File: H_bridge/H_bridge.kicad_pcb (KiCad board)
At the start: 4 copper layers, 100 x 100 mm, 18 parts, among them J1 Conn_01x10_Pin, J10 Conn_Coaxial, J11 Conn_Coaxial, J12 Conn_01x04_Pin, J2 Conn_01x10_Pin, J3 Conn_01x04_Pin, J4 Conn_01x05, J5 Conn_01x03, J6 Conn_Coaxial, J7 Conn_Coaxial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

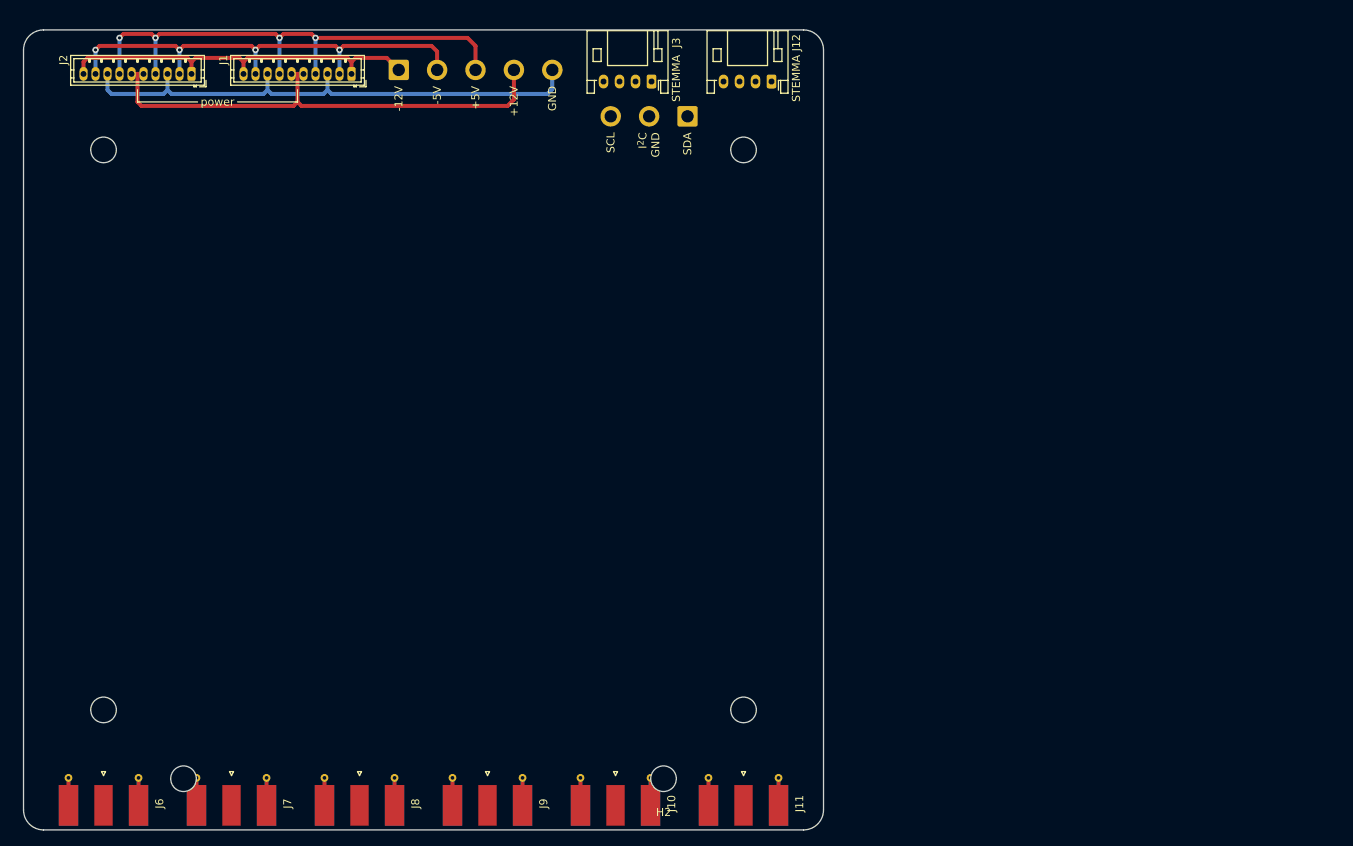
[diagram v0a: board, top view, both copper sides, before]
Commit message: updated 3-channel H-bridge
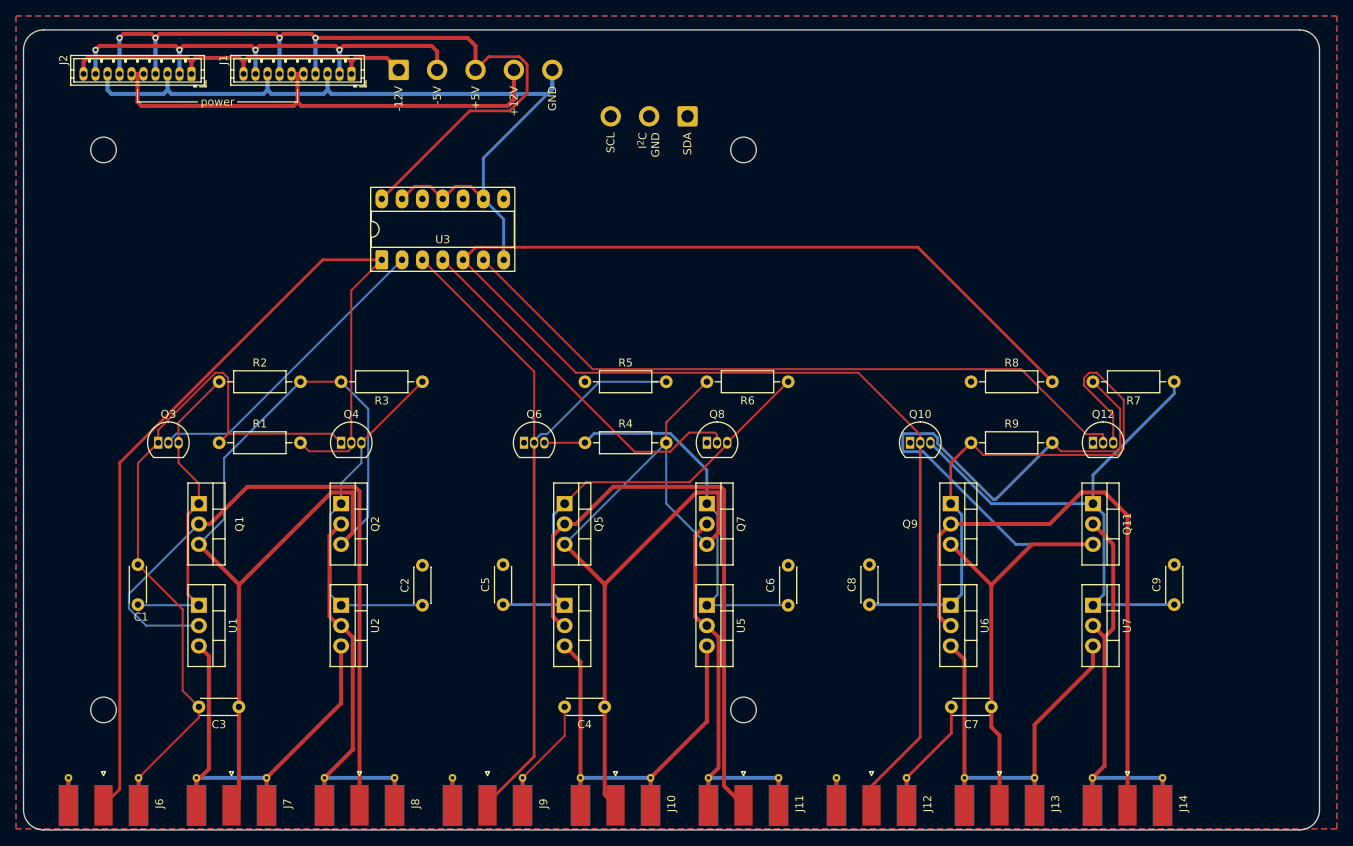
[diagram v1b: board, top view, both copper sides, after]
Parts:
- removed H1, H2: Keystone Electronics 621, matterwaves:Keystone 621
- removed J3: Conn_01x04_Pin, Connector_JST:JST_PH_S4B-PH-K_1x04_P2.00mm_Horizontal
- added C1: 1u, Capacitor_THT:C_Disc_D4.3mm_W1.9mm_P5.00mm, F.Cu at (114.3, 121.8)
- added C2: 1u, Capacitor_THT:C_Disc_D4.3mm_W1.9mm_P5.00mm, F.Cu at (149.9, 121.9)
- added C3: 1u, Capacitor_THT:C_Disc_D4.3mm_W1.9mm_P5.00mm, F.Cu at (126.9, 134.6)
- added C4: 1u, Capacitor_THT:C_Disc_D4.3mm_W1.9mm_P5.00mm, F.Cu at (172.6, 134.6)
- added C5: 1u, Capacitor_THT:C_Disc_D4.3mm_W1.9mm_P5.00mm, F.Cu at (159.9, 121.8)
- added C6: 1u, Capacitor_THT:C_Disc_D4.3mm_W1.9mm_P5.00mm, F.Cu at (195.6, 121.9)
- added C7: 1u, Capacitor_THT:C_Disc_D4.3mm_W1.9mm_P5.00mm, F.Cu at (221.0, 134.6)
- added C8: 1u, Capacitor_THT:C_Disc_D4.3mm_W1.9mm_P5.00mm, F.Cu at (205.7, 121.8)
- added C9: 1u, Capacitor_THT:C_Disc_D4.3mm_W1.9mm_P5.00mm, F.Cu at (243.8, 121.8)
- added J13: Conn_Coaxial, Connector_Coaxial:SMA_Molex_73251-1153_EdgeMount_Horizontal, F.Cu at (222.0, 145.2)
- added J14: Conn_Coaxial, Connector_Coaxial:SMA_Molex_73251-1153_EdgeMount_Horizontal, F.Cu at (238.0, 145.2)
- added Q1: IRF9610, Package_TO_SOT_THT:TO-220-3_Vertical, F.Cu at (121.9, 109.2)
- added Q10: 2N7000, Package_TO_SOT_THT:TO-92_Inline, F.Cu at (210.8, 101.6)
- added Q11: IRF9610, Package_TO_SOT_THT:TO-220-3_Vertical, F.Cu at (233.7, 109.2)
- added Q12: 2N7000, Package_TO_SOT_THT:TO-92_Inline, F.Cu at (233.7, 101.6)
- added Q2: IRF9610, Package_TO_SOT_THT:TO-220-3_Vertical, F.Cu at (139.7, 109.2)
- added Q3: 2N7000, Package_TO_SOT_THT:TO-92_Inline, F.Cu at (116.8, 101.6)
- added Q4: 2N7000, Package_TO_SOT_THT:TO-92_Inline, F.Cu at (139.7, 101.6)
- added Q5: IRF9610, Package_TO_SOT_THT:TO-220-3_Vertical, F.Cu at (167.6, 109.2)
- added Q6: 2N7000, Package_TO_SOT_THT:TO-92_Inline, F.Cu at (162.6, 101.6)
- added Q7: IRF9610, Package_TO_SOT_THT:TO-220-3_Vertical, F.Cu at (185.4, 109.2)
- added Q8: 2N7000, Package_TO_SOT_THT:TO-92_Inline, F.Cu at (185.4, 101.6)
- added Q9: IRF9610, Package_TO_SOT_THT:TO-220-3_Vertical, F.Cu at (215.9, 109.2)
- added R1: 100k, Resistor_THT:R_Axial_DIN0207_L6.3mm_D2.5mm_P10.16mm_Horizontal, F.Cu at (124.5, 101.6)
- added R2: 100k, Resistor_THT:R_Axial_DIN0207_L6.3mm_D2.5mm_P10.16mm_Horizontal, F.Cu at (124.5, 94.0)
- added R3: 100k, Resistor_THT:R_Axial_DIN0207_L6.3mm_D2.5mm_P10.16mm_Horizontal, F.Cu at (149.9, 94.0)
- added R4: 100k, Resistor_THT:R_Axial_DIN0207_L6.3mm_D2.5mm_P10.16mm_Horizontal, F.Cu at (170.2, 101.6)
- added R5: 100k, Resistor_THT:R_Axial_DIN0207_L6.3mm_D2.5mm_P10.16mm_Horizontal, F.Cu at (170.2, 94.0)
- added R6: 100k, Resistor_THT:R_Axial_DIN0207_L6.3mm_D2.5mm_P10.16mm_Horizontal, F.Cu at (195.6, 94.0)
- added R7: 100k, Resistor_THT:R_Axial_DIN0207_L6.3mm_D2.5mm_P10.16mm_Horizontal, F.Cu at (243.8, 94.0)
- added R8: 100k, Resistor_THT:R_Axial_DIN0207_L6.3mm_D2.5mm_P10.16mm_Horizontal, F.Cu at (218.4, 94.0)
- added R9: 100k, Resistor_THT:R_Axial_DIN0207_L6.3mm_D2.5mm_P10.16mm_Horizontal, F.Cu at (218.4, 101.6)
- added U1: IRF510, Package_TO_SOT_THT:TO-220-3_Vertical, F.Cu at (121.9, 121.9)
- added U2: IRF510, Package_TO_SOT_THT:TO-220-3_Vertical, F.Cu at (139.7, 121.9)
- added U3: SN74ACT04N, Package_DIP:DIP-14_W7.62mm_Socket_LongPads, F.Cu at (144.8, 78.7)
- added U4: IRF510, Package_TO_SOT_THT:TO-220-3_Vertical, F.Cu at (167.6, 121.9)
- added U5: IRF510, Package_TO_SOT_THT:TO-220-3_Vertical, F.Cu at (185.4, 121.9)
- added U6: IRF510, Package_TO_SOT_THT:TO-220-3_Vertical, F.Cu at (215.9, 121.9)
- added U7: IRF510, Package_TO_SOT_THT:TO-220-3_Vertical, F.Cu at (233.7, 121.9)
- J12: value Conn_01x04_Pin -> Conn_Coaxial; footprint Connector_JST:JST_PH_S4B-PH-K_1x04_P2.00mm_Horizontal -> Connector_Coaxial:SMA_Molex_73251-1153_EdgeMount_Horizontal
- moved J12 89.6 mm to (206.0, 145.2), turned to 90 degrees
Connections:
- J10 pad 1: unconnected-(J10-In-Pad1) -> VCC2
- J10 pad 2: unconnected-(J10-Ext-Pad2) -> VDD2
- J11 pad 1: unconnected-(J11-In-Pad1) -> Net-(J11-In)
- J11 pad 2: unconnected-(J11-Ext-Pad2) -> Net-(J11-Ext)
- J12 pad 1: /I2C_SCL -> /3A
- J12 pad 2: /I2C_SDA -> GND
- J6 pad 1: unconnected-(J6-In-Pad1) -> /1A
- J6 pad 2: unconnected-(J6-Ext-Pad2) -> GND
- J7 pad 1: unconnected-(J7-In-Pad1) -> VCC1
- J7 pad 2: unconnected-(J7-Ext-Pad2) -> VDD1
- J8 pad 1: unconnected-(J8-In-Pad1) -> Net-(J8-In)
- J8 pad 2: unconnected-(J8-Ext-Pad2) -> Net-(J8-Ext)
- J9 pad 1: unconnected-(J9-In-Pad1) -> /2A
- J9 pad 2: unconnected-(J9-Ext-Pad2) -> GND
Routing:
- net /3A: track 0.00 -> 196.3 mm
- net GND: track 67.7 -> 214.1 mm
- net VCC3: track 0.00 -> 124.9 mm
- net /1A: track 0.00 -> 119.0 mm
- net VCC1: track 0.00 -> 115.0 mm
- net VCC2: track 0.00 -> 103.8 mm
- net /2A: track 0.00 -> 96.2 mm
- net /3Y: track 0.00 -> 87.5 mm
- net Net-(J8-In): track 0.00 -> 85.3 mm
- net Net-(J11-In): track 0.00 -> 76.5 mm
- net Net-(J14-In): track 0.00 -> 75.3 mm
- net /logic31: track 0.00 -> 75.2 mm
- net /logic30: track 0.00 -> 67.0 mm
- net /logic21: track 0.00 -> 56.0 mm
- net /logic20: track 0.00 -> 50.9 mm
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- added copper zone on B.Cu, net GND
- added copper zone on F.Cu, net GND
- added copper zone on In1.Cu, net GND
- added copper zone on In2.Cu, net GND
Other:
- board size 100 x 100 mm -> 162 x 100 mm
- board text added: "3 channel H-bridge"
- board text added: "Mueller Group, UC Berkeley"
- board text removed: "CIRCUIT NAME"
- board text removed: "J Roth, Mueller Group, UC Berkeley"
- board text removed: "STEMMA"
- board text removed: "err"
